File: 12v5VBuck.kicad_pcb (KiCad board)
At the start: 4 copper layers, 20.5 x 26.4 mm, 16 parts, among them IC1 TPS54302DDCT, J1 Conn_01x02, J2 Conn_01x02

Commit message: Added a few more gnd vias
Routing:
- net GND: vias 32 -> 38
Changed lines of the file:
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@@
   (via (at 66.3 21.5) (size 0.6) (drill 0.3) (layers "F.Cu" "B.Cu") (net 2))
   (via (at 60.5 30.7) (size 0.6) (drill 0.3) (layers "F.Cu" "B.Cu") (net 2))
+  (via (at 56.3 15.6) (size 0.6) (drill 0.3) (layers "F.Cu" "B.Cu") (net 2))
   (via (at 61.7 28.6) (size 0.6) (drill 0.3) (layers "F.Cu" "B.Cu") (net 2))
   (via (at 65.81 23.21) (size 0.6) (drill 0.3) (layers "F.Cu" "B.Cu") (net 2))
@@
   (via (at 71.7 31.8) (size 0.6) (drill 0.3) (layers "F.Cu" "B.Cu") (net 2))
   (via (at 68.4 20) (size 1.2) (drill 0.6) (layers "F.Cu" "B.Cu") (net 2))
+  (via (at 55.9 38.7) (size 0.6) (drill 0.3) (layers "F.Cu" "B.Cu") (net 2))
   (via (at 59.4 29.4) (size 0.6) (drill 0.3) (layers "F.Cu" "B.Cu") (net 2))
   (via (at 56 31) (size 0.6) (drill 0.3) (layers "F.Cu" "B.Cu") (net 2))
   (via (at 70.983247 29.81634) (size 0.6) (drill 0.3) (layers "F.Cu" "B.Cu") (net 2))
   (via (at 62.1 31.6) (size 0.6) (drill 0.3) (layers "F.Cu" "B.Cu") (net 2))
+  (via (at 74 39.1) (size 0.6) (drill 0.3) (layers "F.Cu" "B.Cu") (net 2))
   (via (at 68.5 21.4) (size 0.6) (drill 0.3) (layers "F.Cu" "B.Cu") (net 2))
   (via (at 67.1 16) (size 0.6) (drill 0.3) (layers "F.Cu" "B.Cu") (net 2))
@@
   (via (at 62.5 26) (size 0.6) (drill 0.3) (layers "F.Cu" "B.Cu") (net 2))
   (via (at 64.7 21.1) (size 0.6) (drill 0.3) (layers "F.Cu" "B.Cu") (net 2))
+  (via (at 74.1 33.8) (size 0.6) (drill 0.3) (layers "F.Cu" "B.Cu") (net 2))
   (via (at 56.5 36) (size 0.6) (drill 0.3) (layers "F.Cu" "B.Cu") (net 2))
   (via (at 62.6 16.7) (size 0.6) (drill 0.3) (layers "F.Cu" "B.Cu") (net 2))
+  (via (at 65.3 35.6) (size 0.6) (drill 0.3) (layers "F.Cu" "B.Cu") (net 2))
+  (via (at 59.2 15.6) (size 0.6) (drill 0.3) (layers "F.Cu" "B.Cu") (net 2))
   (via (at 73.9675 26.3) (size 0.6) (drill 0.3) (layers "F.Cu" "B.Cu") (net 2))
   (via (at 74.5 20.6) (size 0.6) (drill 0.3) (layers "F.Cu" "B.Cu") (net 2))
@@
     )
   )
-  (group "" (id 94d17fd6-2a15-4bf5-a0a4-f16847105116)
-    (members
-      0224078f-4e85-4b56-97d3-5c55b2edced0
-      02dc2a5c-61ef-49db-a3cb-37bcee863e7a
-      03d6d9b0-0b2b-4ba2-bda3-9c8d34610942
-      0419b6eb-674e-4af8-b0fb-e724d592288a
-      0421a7ef-436a-41c3-a899-6b4958ca76b3
-      069e5cb1-e7f4-4dba-a2c2-fa1372e07adb
-      09e8f0c6-6270-48ab-8318-600105c8eca4
-      09f5721f-d5ba-47af-9fb5-4c1727abda6e
-      0a63c416-5706-4209-ad93-c04fbfb50a1f
-      0e0f822c-cc62-4823-8f07-c7bf29eb94f9
-      0ef22faa-9dc5-4b6b-9544-81d865794ee7
-      0f67d251-32fe-4955-a86f-88d9b342bcd4
-      11440e30-dcd6-4fd2-a73f-6c955a798666
-      11c60416-3163-414e-bb61-ba7b86e5c478
-      13013620-6db7-49a8-ab2e-04b1e85e5b09
-      13d014e5-5551-49a7-b72c-6723f2bfe2c8
-      150be7e1-b694-483e-8ff8-f1fb69c685be
-      152f5f24-1909-4e23-b04b-da15fda12587
-      1669e921-b2d3-4dda-8b2f-c08321762730
-      168824e3-a727-4932-be27-74049cdbd901
-      176e3f23-9043-4639-b885-16c21d3ebf3f
-      19a8d2ce-a3bd-4b6f-b9fa-f0d0fd096d9b
-      1a751863-4fbb-4697-b6aa-65b1d83d4578
-      204f6718-0830-41f1-9fa2-ed73be5256cc
-      207d43b7-ba35-45cf-b4a5-f7b7f0b9c863
-      20a46961-aad8-4282-b564-491b362366bb
-      20f85828-f2db-4e1f-84b4-8c25ae456492
-      22cb54e9-00f4-4a0f-b632-e25b7a2dbbe6
-      236dc34e-3768-4365-80aa-7a83f9702c0a
-      245fe0ea-4179-40d3-81f6-131a5d45eef0
-      25bc0953-90c2-4fae-b035-9fb7bd3e8f51
-      2b353849-42df-4f52-8804-43c5d5bb646b
-      2ce60a9d-776c-4605-8d77-e569394239db
-      309aad35-7fd4-4765-b379-e130ca77ca5e
-      31f83094-7b13-4b9f-965a-c5ac28f18574
-      33581b50-51e3-4aa4-b894-ba5295bde0a0
-      3627816f-1520-49ff-b039-027b86ffa16d
-      3a0114b5-0881-41e6-b48c-01d0f9ca2e49
-      41cea99b-e0f3-441f-b222-c5244d3e9d1a
-      41ecab6c-45b8-46b4-b961-89550861ea15
-      42ee4f19-4cbf-4045-a2f9-d7fc1e9ff7d8
-      434b38ce-050f-43e9-8866-3745aa3a2a61
-      44fdeb94-4a8f-42ba-a3f8-f813a50482f2
-      469e5497-a7d3-4728-ac92-9460164fc15f
-      494905e3-3c3c-49da-89ed-c92b50782b9d
-      49ad9878-c995-459b-b11a-15ae18037852
-      4a14a7f5-6069-4d45-878f-426c3558541a
-      50906472-1f86-4d6c-8f32-030fcbcabf97
-      52c5003c-9dbc-4c87-9776-4ea86bcb19f8
-      53689bb4-1c31-4e1f-bca7-2ba6a4598818
-      53de3a18-0d0f-44af-9612-519a149890c5
-      5d5c7590-acc3-435b-959e-05730c3f4602
-      5f74d6df-7548-43c4-b432-ed519d1c14a5
-      605eec76-c42c-4d40-a493-89a21292b19d
-      6314f348-d5aa-4da4-936c-041e577322a2
-      65ec91a4-1e47-4eea-8b51-0a2b156b8b7e
-      6710618e-c272-47bd-9f58-1aa3d894a8b8
-      67b07275-5ee5-4f6c-8cb6-b43903400030
-      6b46fe51-ee11-4803-8e16-25113ea50163
-      6c94f0e6-4f0f-43ab-9f84-12c2af088378
-      705e64ec-2554-4b85-920e-ca014c8afd88
-      744806d1-cc3a-4408-8c16-0af62dd3dbe0
-      747133c5-e3f8-4220-ae0d-2f9ac9d55e1f
-      75308ea5-84a4-4109-aa77-dae870617d32
-      754d16fc-222f-453e-93b4-975d27bd3b93
-      75fcbb0b-478c-4f8d-98f3-2d2f48795615
-      77e92e70-cf55-426c-b4fd-8acd34580d55
-      79d5c596-9fe5-446f-9e9b-c4aed785634c
-      7c059284-e1ef-4f70-9578-5159d4a3f8fa
-      7f3ec9a2-dc69-4a87-a822-46d348f8944c
-      813426f4-3fd0-473d-915d-4e5ab01c2249
-      851e2fbd-e121-4e81-ad44-d807ea2d9018
-      871eca4c-e814-4a95-a158-ce3bace7587c
-      887eb96c-9f0c-4fdb-a908-af6ed257d4b4
-      8aed4108-a5b5-426b-84dd-0d22fe565966
-      953f7926-6ad0-4b2a-8da6-9bd5f3a2e9be
-      9696cf1d-15bb-406e-8071-be7a05f08769
-      977d1ec7-0031-413d-9e0f-6d78d554e525
-      9825e2e0-353f-4c13-9790-b62c91c0236c
-      9b657a65-737c-41fa-a535-90d64daa04ee
-      9bd384f3-0129-4b97-9f4f-a978c67b3f8f
-      9de007d5-37f0-41e8-9c53-b82729154741
-      9fb1007c-e2b3-42fd-b177-02f598563e88
-      a9728d6e-a00a-4a90-81ed-163f3fbc3398
-      ac02e11c-24f7-44ae-bfe0-a5c05a3c818a
-      ada3027d-b100-4fc2-a44d-6652b16334e1
-      b1027aa1-58ee-434b-8177-7b4ba3aad1b1
-      b1505b42-5b79-40fa-bb05-efcb2e887584
-      b30144d0-9c4a-477a-9b9b-1d10155d5033
-      b8ad3f75-61ad-4b65-ba4d-15a03d9a252a
-      ba5d8726-9640-4d77-809e-7bbc3a02b3a1
-      ba7b70dc-22ae-47a4-8c8c-a338799c5940
-      bcd23af4-fd33-40a8-b2af-fbd07518b3ab
-      bcf1668e-6507-428f-8ab1-2eb24bc4e1b6
-      bfdede4a-8cf0-4017-ad4f-393152e17a8e
-      c219e655-fd10-48ff-b3e2-1350204380f7
-      c2bf97c9-d36b-41eb-b2f5-1aba2a2f538c
-      c56c3088-ce7a-4e97-b723-0ab178dda9ba
-      c85cae85-484c-4d99-98e1-f18f30816d71
-      ca9a6de5-791d-4038-911a-39a05cfa6511
-      cac3332f-b30f-40b8-89e3-7a776fe810d3
-      cb5b3f14-5d5d-4dfc-af78-d1d1a67b87f1
-      cbbb90cb-8260-48e6-ab13-66417dbc4563
-      cf66b7f4-0d9a-43db-b90e-959af144923b
-      d027f6c4-8c37-4ed3-98a1-aa51e4d48b70
-      d221ea11-eb37-49b9-8477-082b44d6b2fe
-      d24732dc-4933-4fa0-a4ae-63a152127d72
-      d6c1e1da-0431-4b11-ae30-2aba8e94b0e2
-      dbe46752-f477-4456-877b-af6fcbb3601d
-      dfe921ca-75f2-4da4-9897-330b052be61f
-      e117606b-c946-43ab-96c4-6bf53765e117
-      e76ab50d-7de9-48c4-93c4-a086cfeea4e3
-      e862d873-41a7-4267-bf09-f52bfc02813c
-      eef28f76-a99b-4597-811c-b5e5a7d3206f
-      f3807244-b7b9-4345-b204-7e53236ff562
-      f5a0fd75-9971-4ccf-a6c0-ee1c0e35a0b1
-      f75b8c5a-76bd-49f0-859a-8a78daf7cc58
-      f7d9deb9-03c4-49ad-885e-65fba68c1d2f
-      f7fb9853-04cf-4227-8ae4-71b5600d2e40
-      fc569787-e33e-4008-bb95-1e76efaa05f6
-      fcbeb128-9581-43a5-bd9b-2d7189cde3e8
-      fd2b441a-c360-4744-97d9-cb2ff16810e3
-      fe9a859d-8fce-44e0-b3d1-503c595fe0c8
-      feccd340-f417-4614-a7aa-e9c637355cc7
-    )
-  )

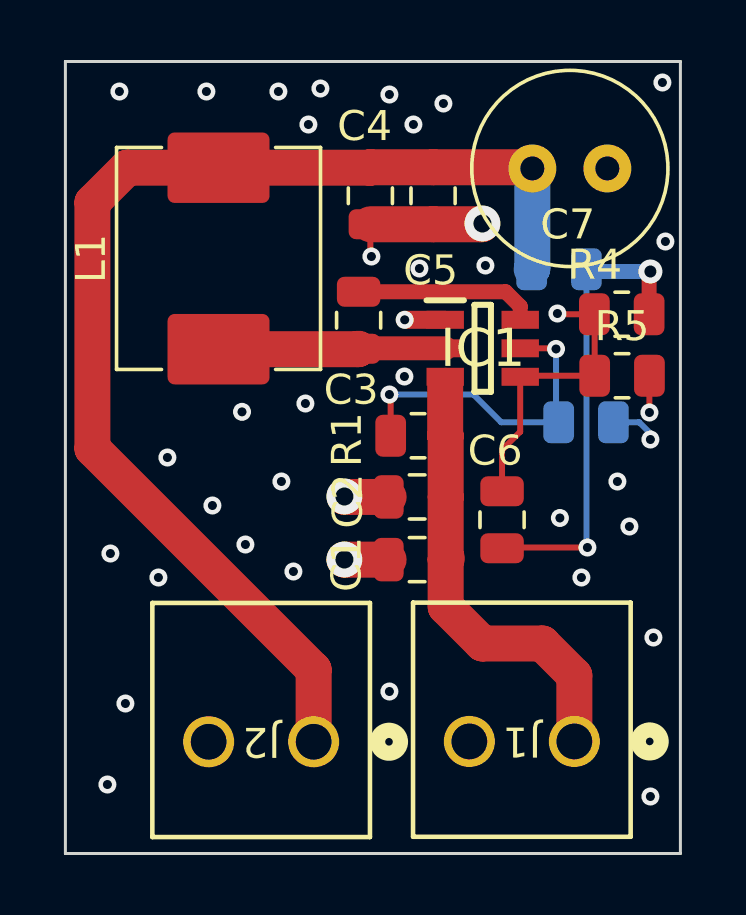
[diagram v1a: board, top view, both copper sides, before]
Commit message: Added a mounting hole
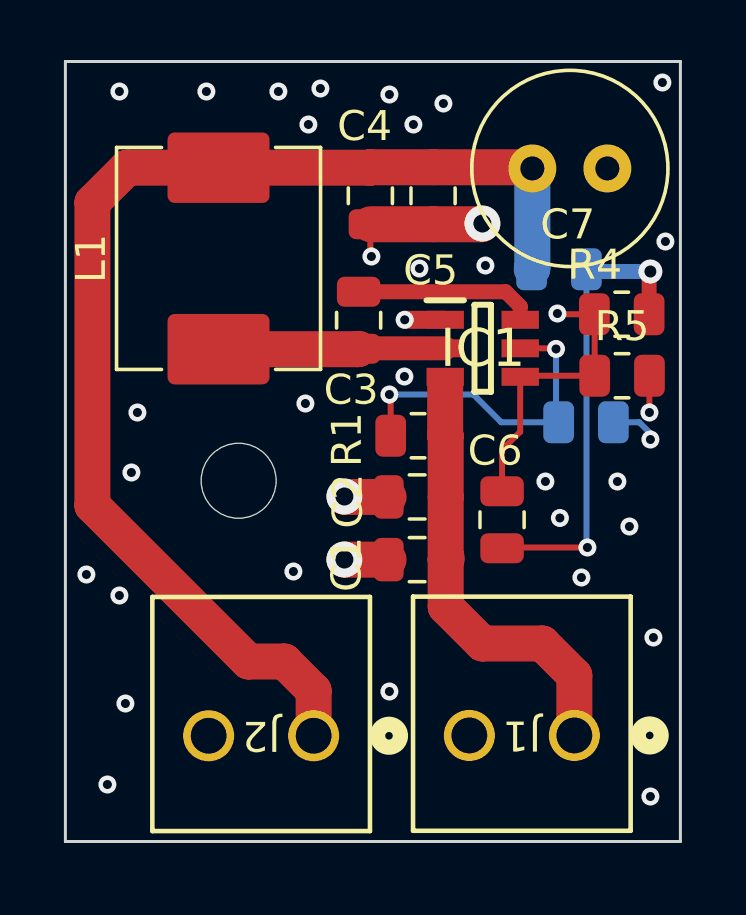
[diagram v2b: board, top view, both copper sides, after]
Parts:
- added H1: MountingHole, MountingHole:MountingHole_2.5mm, F.Cu at (60.3, 28.6)
- moved J1 0.20 mm to (71.5, 37.1)
- moved J2 0.20 mm to (62.8, 37.1)
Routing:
- net +5V: track 39.3 -> 39.8 mm
- net GND: vias 38 -> 36
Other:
- board size 20.5 x 26.4 mm -> 20.5 x 26 mm
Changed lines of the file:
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@@
   )
   (footprint "footprints:CONN_1984617_PXC" (layer "F.Cu")
-    (at 62.775 37.275 180)
+    (at 62.775 37.075 180)
     (tags "1984617 ")
     (property "Sheetfile" "12v5VBuck.kicad_sch")
@@
       (rotate (xyz 0 0 0))
     )
-    (model "C:/Users/Sylvester Pudelko/Documents/KiCad/7.0/3dmodels/DDC0006A.stp"
-      (offset (xyz 0 0 0))
-      (scale (xyz 1 1 1))
-      (rotate (xyz 0 0 0))
-    )
   )
   (footprint "Capacitor_SMD:C_0805_2012Metric" (layer "F.Cu")
@@
     )
   )
+  (footprint "MountingHole:MountingHole_2.5mm" (layer "F.Cu")
+    (at 60.275 28.575)
+    (descr "Mounting Hole 2.5mm, no annular")
+    (tags "mounting hole 2.5mm no annular")
+    (property "Sheetfile" "12v5VBuck.kicad_sch")
+    (property "Sheetname" "")
+    (property "ki_description" "Mounting Hole without connection")
+    (property "ki_keywords" "mounting hole")
+    (attr exclude_from_pos_files)
+    (fp_text reference "H1" (at 0 -3.5) (layer "F.SilkS") hide
+        (effects (font (size 1 1) (thickness 0.15)))
+    )
+    (fp_text value "MountingHole" (at 0 3.5) (layer "F.Fab") hide
+        (effects (font (size 1 1) (thickness 0.15)))
+    )
+    (fp_text user "${REFERENCE}" (at 0 0) (layer "F.Fab")
+        (effects (font (size 1 1) (thickness 0.15)))
+    )
+    (fp_circle (center 0 0) (end 2.5 0)
+      (stroke (width 0.15) (type solid)) (fill none) (layer "Cmts.User"))
+    (fp_circle (center 0 0) (end 2.75 0)
+      (stroke (width 0.05) (type solid)) (fill none) (layer "F.CrtYd"))
+    (pad "" np_thru_hole circle (at 0 0) (size 2.5 2.5) (drill 2.5) (layers "*.Cu" "*.Mask"))
+  )
   (footprint "Resistor_SMD:R_0805_2012Metric" (layer "F.Cu")
     (at 73.045 23.025 180)
@@
   )
   (footprint "footprints:CONN_1984617_PXC" (layer "F.Cu")
-    (at 71.465 37.265 180)
+    (at 71.465 37.065 180)
     (tags "1984617 ")
     (property "Sheetfile" "12v5VBuck.kicad_sch")
@@
     )
   )
-  (gr_rect (start 54.5 14.6) (end 75 41)
+  (gr_rect (start 54.5 14.6) (end 75 40.6)
     (stroke (width 0.1) (type default)) (fill none) (layer "Edge.Cuts"))
   (segment (start 67.16 27.0675) (end 67.16 25.41) (width 1.2) (layer "F.Cu") (net 1))
   (segment (start 67.175 29.115) (end 67.175 27.0825) (width 1.2) (layer "F.Cu") (net 1))
+  (segment (start 71.465001 35.065001) (end 71.465001 37.065) (width 1.2) (layer "F.Cu") (net 1))
   (segment (start 67.1675 27.075) (end 67.16 27.0675) (width 1.2) (layer "F.Cu") (net 1))
-  (segment (start 71.465001 37.265) (end 71.465001 35.065001) (width 1.2) (layer "F.Cu") (net 1))
   (segment (start 67.175 27.0825) (end 67.1675 27.075) (width 1.2) (layer "F.Cu") (net 1))
   (segment (start 67.175 31.205) (end 67.175 29.115) (width 1.2) (layer "F.Cu") (net 1))
@@
   (via (at 65.8 25.1) (size 0.6) (drill 0.3) (layers "F.Cu" "B.Cu") (net 2))
   (via (at 66.3 21.5) (size 0.6) (drill 0.3) (layers "F.Cu" "B.Cu") (net 2))
-  (via (at 60.5 30.7) (size 0.6) (drill 0.3) (layers "F.Cu" "B.Cu") (net 2))
+  (via (at 56.9 26.3) (size 0.6) (drill 0.3) (layers "F.Cu" "B.Cu") (net 2))
   (via (at 56.3 15.6) (size 0.6) (drill 0.3) (layers "F.Cu" "B.Cu") (net 2))
-  (via (at 61.7 28.6) (size 0.6) (drill 0.3) (layers "F.Cu" "B.Cu") (net 2))
   (via (at 65.81 23.21) (size 0.6) (drill 0.3) (layers "F.Cu" "B.Cu") (net 2))
-  (via (at 57.9 27.8) (size 0.6) (drill 0.3) (layers "F.Cu" "B.Cu") (net 2))
+  (via (at 56.7 28.3) (size 0.6) (drill 0.3) (layers "F.Cu" "B.Cu") (net 2))
   (via (at 63 15.5) (size 0.6) (drill 0.3) (layers "F.Cu" "B.Cu") (net 2))
   (via (at 71.7 31.8) (size 0.6) (drill 0.3) (layers "F.Cu" "B.Cu") (net 2))
   (via (at 68.4 20) (size 1.2) (drill 0.6) (layers "F.Cu" "B.Cu") (net 2))
   (via (at 55.9 38.7) (size 0.6) (drill 0.3) (layers "F.Cu" "B.Cu") (net 2))
-  (via (at 59.4 29.4) (size 0.6) (drill 0.3) (layers "F.Cu" "B.Cu") (net 2))
-  (via (at 56 31) (size 0.6) (drill 0.3) (layers "F.Cu" "B.Cu") (net 2))
+  (via (at 56.3 32.4) (size 0.6) (drill 0.3) (layers "F.Cu" "B.Cu") (net 2))
   (via (at 70.983247 29.81634) (size 0.6) (drill 0.3) (layers "F.Cu" "B.Cu") (net 2))
   (via (at 62.1 31.6) (size 0.6) (drill 0.3) (layers "F.Cu" "B.Cu") (net 2))
@@
   (via (at 72.9 28.6) (size 0.6) (drill 0.3) (layers "F.Cu" "B.Cu") (net 2))
   (via (at 74.4 15.3) (size 0.6) (drill 0.3) (layers "F.Cu" "B.Cu") (net 2))
-  (via (at 60.386946 26.278265) (size 0.6) (drill 0.3) (layers "F.Cu" "B.Cu") (net 2))
+  (via (at 70.5 28.6) (size 0.6) (drill 0.3) (layers "F.Cu" "B.Cu") (net 2))
   (via (at 66.1 16.7) (size 0.6) (drill 0.3) (layers "F.Cu" "B.Cu") (net 2))
   (via (at 73.3 30.1) (size 0.6) (drill 0.3) (layers "F.Cu" "B.Cu") (net 2))
   (via (at 63.8 29.1) (size 1.2) (drill 0.6) (layers "F.Cu" "B.Cu") (net 2))
-  (via (at 57.6 31.8) (size 0.6) (drill 0.3) (layers "F.Cu" "B.Cu") (net 2))
+  (via (at 55.2 31.7) (size 0.6) (drill 0.3) (layers "F.Cu" "B.Cu") (net 2))
   (via (at 63.8 31.2) (size 1.2) (drill 0.6) (layers "F.Cu" "B.Cu") (net 2))
   (via (at 61.6 15.6) (size 0.6) (drill 0.3) (layers "F.Cu" "B.Cu") (net 2))
@@
   (segment (start 70.8546 26.4371) (end 71.0425 26.625) (width 0.2) (layer "B.Cu") (net 7))
   (segment (start 69.025 26.625) (end 70.9425 26.625) (width 0.2) (layer "B.Cu") (net 7))
-  (segment (start 62.775001 34.875001) (end 55.4 27.5) (width 1.2) (layer "F.Cu") (net 8))
+  (segment (start 61.8 34.6) (end 60.6 34.6) (width 1.2) (layer "F.Cu") (net 8))
+  (segment (start 64.65 18.14) (end 64.665 18.125) (width 1.2) (layer "F.Cu") (net 8))
+  (segment (start 62.775001 37.075) (end 62.775001 35.575001) (width 1.2) (layer "F.Cu") (net 8))
+  (segment (start 55.4 19.3) (end 56.56 18.14) (width 1.2) (layer "F.Cu") (net 8))
+  (segment (start 60.6 34.6) (end 55.4 29.4) (width 1.2) (layer "F.Cu") (net 8))
+  (segment (start 66.755 18.125) (end 70.025 18.125) (width 1.2) (layer "F.Cu") (net 8))
+  (segment (start 59.905 18.14) (end 64.65 18.14) (width 1.2) (layer "F.Cu") (net 8))
+  (segment (start 55.4 29.4) (end 55.4 19.3) (width 1.2) (layer "F.Cu") (net 8))
+  (segment (start 62.775001 35.575001) (end 61.8 34.6) (width 1.2) (layer "F.Cu") (net 8))
   (segment (start 56.56 18.14) (end 59.605 18.14) (width 1.2) (layer "F.Cu") (net 8))
-  (segment (start 55.4 19.3) (end 56.56 18.14) (width 1.2) (layer "F.Cu") (net 8))
-  (segment (start 64.65 18.14) (end 64.665 18.125) (width 1.2) (layer "F.Cu") (net 8))
-  (segment (start 55.4 27.5) (end 55.4 19.3) (width 1.2) (layer "F.Cu") (net 8))
-  (segment (start 66.755 18.125) (end 70.025 18.125) (width 1.2) (layer "F.Cu") (net 8))
-  (segment (start 62.775001 37.275) (end 62.775001 34.875001) (width 1.2) (layer "F.Cu") (net 8))
-  (segment (start 59.905 18.14) (end 64.65 18.14) (width 1.2) (layer "F.Cu") (net 8))
   (segment (start 70.025 18.125) (end 70.065 18.165) (width 1.2) (layer "F.Cu") (net 8))
   (segment (start 64.665 18.125) (end 66.755 18.125) (width 1.2) (layer "F.Cu") (net 8))
